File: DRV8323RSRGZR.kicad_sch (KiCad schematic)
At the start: 39 parts, among them Q10 TPH3R704PL, Q11 TPH3R704PL, Q12 TPH3R704PL, Q7 TPH3R704PL, Q8 TPH3R704PL, Q9 TPH3R704PL, U2 TLV76733DRVR, U5 DRV8323RSRGZR

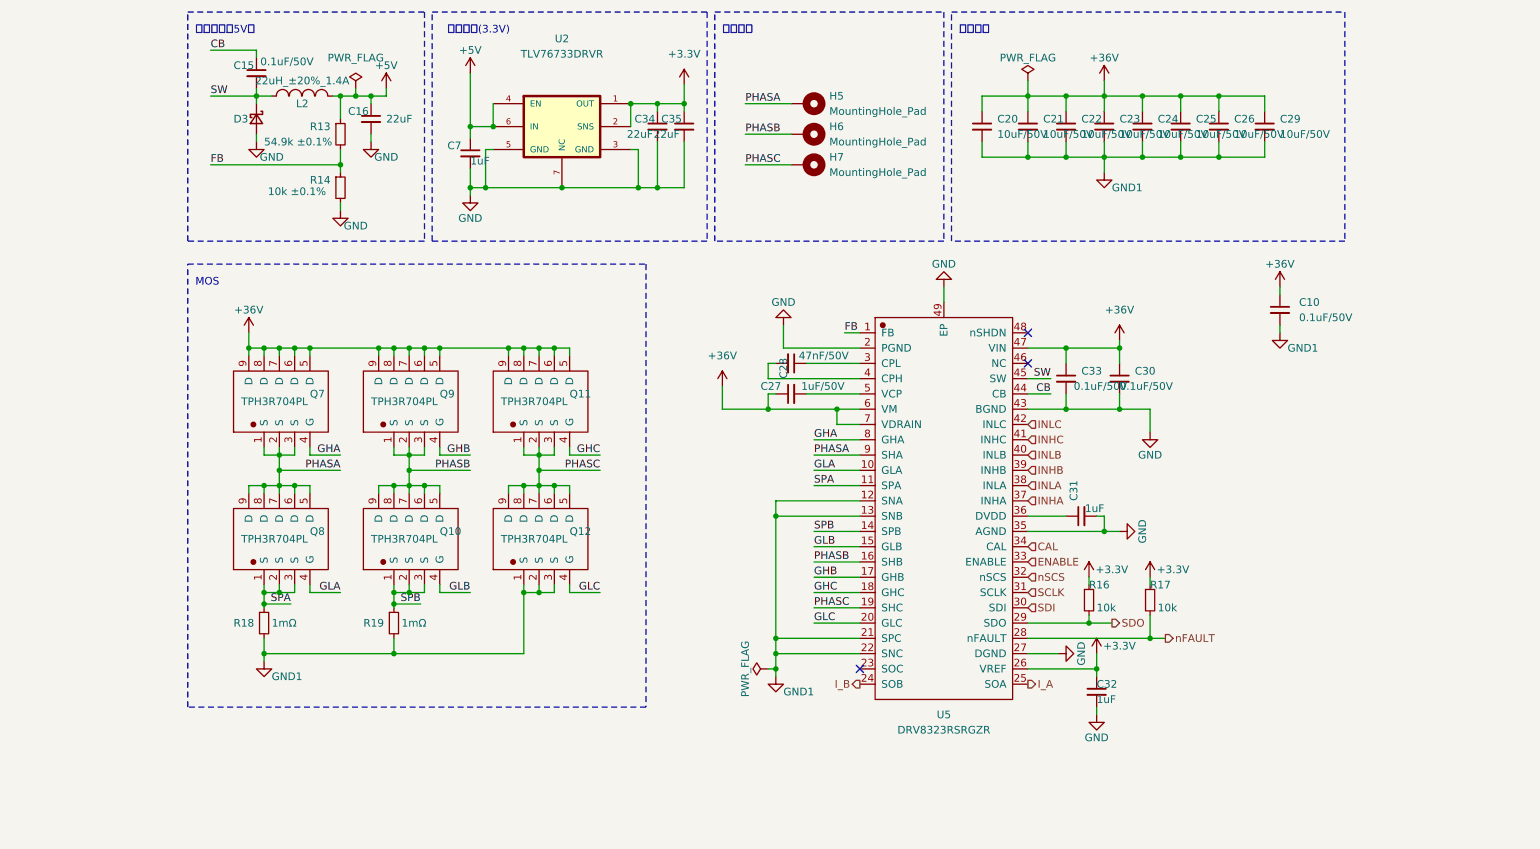
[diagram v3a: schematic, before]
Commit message: 升级主控STM32G474，增加AS5047P编码器，支持NTC温度采样
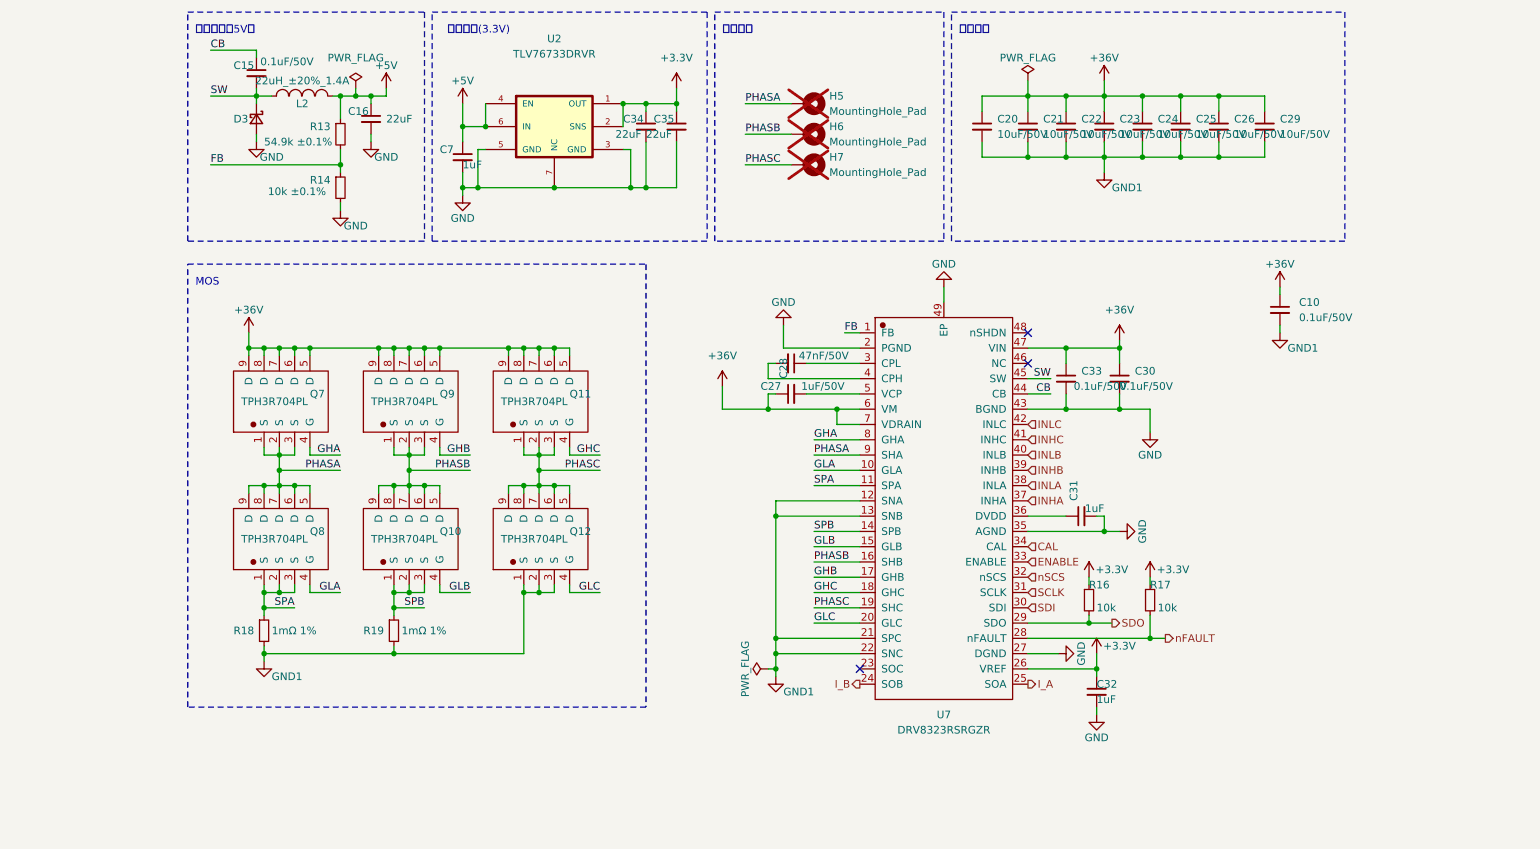
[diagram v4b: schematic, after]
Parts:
- removed U5: DRV8323RSRGZR, Rick_Drive:DRV8323RS_QFN-48-EP(7x7), symbol Rick_Drive:DRV8323RSRGZR
- added U7: DRV8323RSRGZR, Rick_Drive:DRV8323RS_QFN-48-EP(7x7), symbol Rick_Drive:DRV8323RSRGZR
- H5, H6, H7: now not fitted
- R18, R19: value 1mΩ -> 1mΩ 1%
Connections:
- net +3.3V: now also U7.26 (VREF)
- net +36V: now also U7.47 (VIN), U7.6 (VM), U7.7 (VDRAIN)
- net CAL: now also U7.34 (CAL)
- net CB: now also U7.44 (CB)
- net ENABLE: now also U7.33 (ENABLE)
- net FB: now also U7.1 (FB)
- net GHA: now also U7.8 (GHA)
- net GHB: now also U7.17 (GHB)
- net GHC: now also U7.18 (GHC)
- net GLA: now also U7.10 (GLA)
- net GLB: now also U7.15 (GLB)
- net GLC: now also U7.20 (GLC)
- net GND: now also U7.2 (PGND), U7.27 (DGND), U7.35 (AGND), U7.43 (BGND), U7.49 (EP)
- net GND1: now also U7.12 (SNA), U7.13 (SNB), U7.21 (SPC), U7.22 (SNC)
- net INHA: now also U7.37 (INHA)
- net INHB: now also U7.39 (INHB)
- net INHC: now also U7.41 (INHC)
- net INLA: now also U7.38 (INLA)
- net INLB: now also U7.40 (INLB)
- net INLC: now also U7.42 (INLC)
- net I_A: now also U7.25 (SOA)
- net I_B: now also U7.24 (SOB)
- net PHASA: now also U7.9 (SHA)
- net PHASB: now also U7.16 (SHB)
- net PHASC: now also U7.19 (SHC)
- net SCLK: now also U7.31 (SCLK)
- net SDI: now also U7.30 (SDI)
- net SDO: now also U7.29 (SDO)
- net SPA: now also U7.11 (SPA)
- net SPB: now also U7.14 (SPB)
- net SW: now also U7.45 (SW)
- net nFAULT: now also U7.28 (nFAULT)
- net nSCS: now also U7.32 (nSCS)
- net at C31.1: now also U7.36 (DVDD)
- net at C27.1: now also U7.3 (CPL)
- net at C27.2: now also U7.4 (CPH)
- net at C28.2: now also U7.5 (VCP)
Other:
- moved on the sheet: C34, C35, C7, R18, R19, U2
